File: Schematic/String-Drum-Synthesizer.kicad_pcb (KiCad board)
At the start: 2 copper layers, 62 parts, among them U1 LM1117MP-3.3, U2 SII1136CTU, U4 LM3900DR, U5 LM1117MP-3.3, U6 STM32F722RCTx

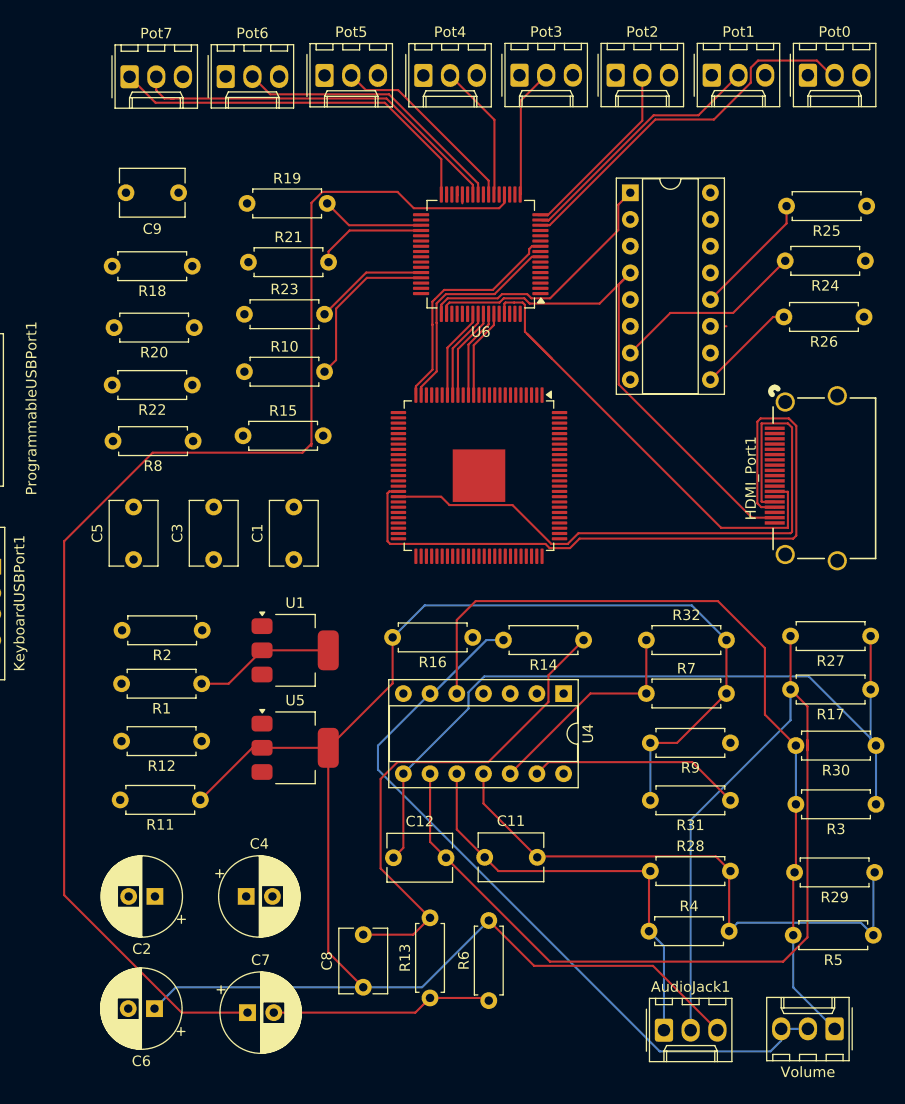
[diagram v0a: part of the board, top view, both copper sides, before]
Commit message: Deleted old traces
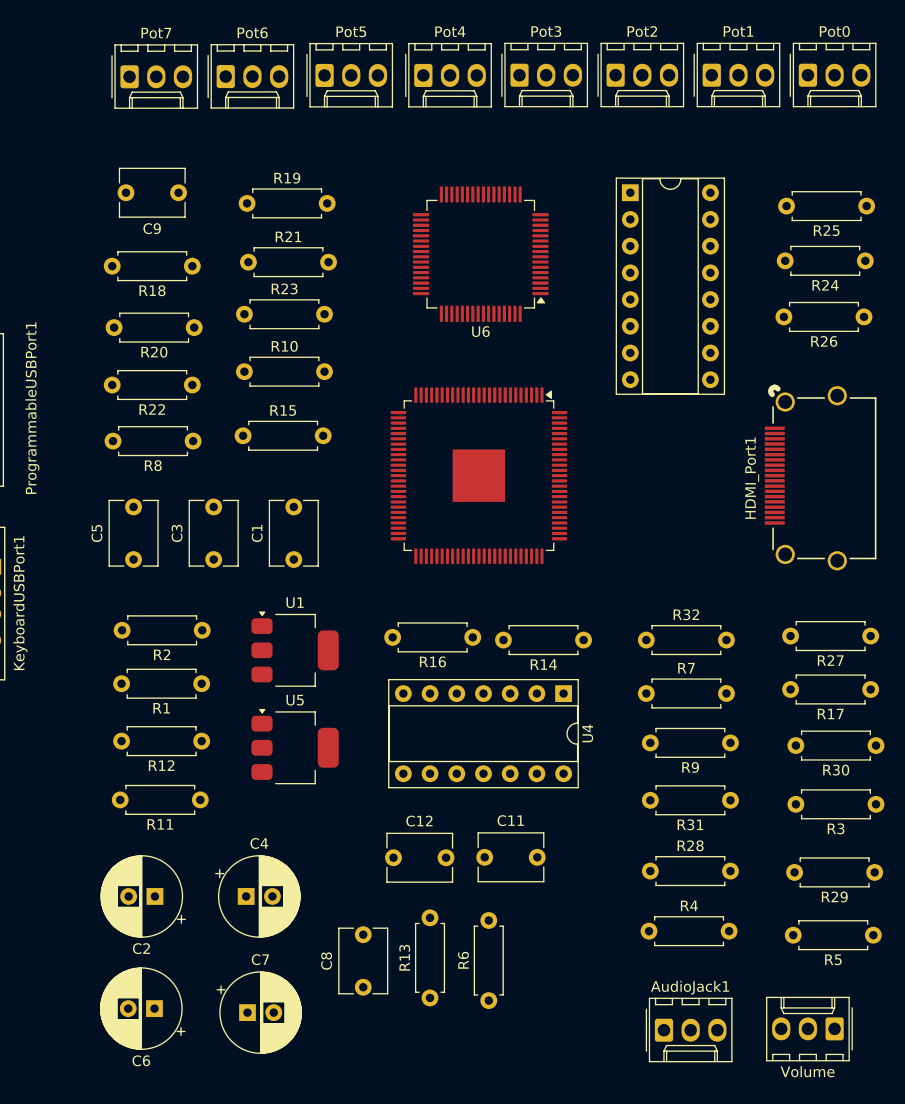
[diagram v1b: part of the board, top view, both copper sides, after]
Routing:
- net +2V5: track 168.1 -> 0.00 mm
- net /DAC Out: track 126.7 -> 0.00 mm
- net /Audio Out R: track 114.7 -> 0.00 mm
- net /AmplifiedSignal: track 78.1 -> 0.00 mm
- net Net-(U4-3IN-): track 77.3 -> 0.00 mm
- net Net-(Pot8-Pin_2): track 72.2 -> 0.00 mm
- net /DSDA: track 69.5 -> 0.00 mm
- net /DSCL: track 61.5 -> 0.00 mm
- net Net-(U4-IN4-): track 55.6 -> 0.00 mm
- net /HDMI_PWR: track 51.1 -> 0.00 mm
- net +3V3: track 49.6 -> 0.00 mm
- net Net-(C8-Pad2): track 48.4 -> 0.00 mm
- net /PB8: track 46.3 -> 0.00 mm
- net /Audio Out L: track 41.3 -> 0.00 mm
- net /EmotiveKnobValue7: track 36.3 -> 0.00 mm
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
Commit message: SCHEMATIC COMPLETE
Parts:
- removed 74LS257: 74LS257, Package_DIP:DIP-16_W7.62mm_Socket
- removed R26: 1M, Resistor_THT:R_Axial_DIN0207_L6.3mm_D2.5mm_P7.62mm_Horizontal
- added R33: 5.6k, Resistor_THT:R_Axial_DIN0207_L6.3mm_D2.5mm_P7.62mm_Horizontal, F.Cu at (145.9, 76.2)
- R24: value 1M -> 4k7
- R25: value 1M -> 10k
- moved R17 22.7 mm to (168.3, 129.3)
- moved R27 22.7 mm to (168.3, 124.2)
- moved Volume 21.3 mm to (143.6, 138.4)
- moved R24 15.0 mm to (156.5, 56.0), turned to 0 degrees
- moved R5 11.7 mm to (167.6, 118.2)
- moved R29 11.7 mm to (167.8, 112.3)
- moved R25 11.6 mm to (156.5, 60.1), turned to 0 degrees
- moved R30 10.5 mm to (167.5, 101.5)
- moved R3 10.5 mm to (167.5, 107.1)
- moved KeyboardUSBPort1 9.31 mm to (82.3, 107.7)
- moved R1 0.85 mm to (104.8, 105.2)
- moved HDMI_Port1 0.83 mm to (164.7, 86.0)
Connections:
- net /PC13 renamed /NRESET
- HDMI_Port1 pad 1: /PB6 -> /TX2+
- HDMI_Port1 pad 10: /PB10 -> /TXC+
- HDMI_Port1 pad 11: unconnected-(HDMI_Port1-Pad11) -> GND
- HDMI_Port1 pad 12: /PB11 -> /TXC-
- HDMI_Port1 pad 18: /HDMI_PWR -> +5V
- HDMI_Port1 pad 19: unconnected-(HDMI_Port1-Pad19) -> Net-(HDMI_Port1-Pad19)
- HDMI_Port1 pad 2: unconnected-(HDMI_Port1-Pad2) -> GND
- HDMI_Port1 pad 3: /PB7 -> /TX2-
- HDMI_Port1 pad 4: /PB4 -> /TX1+
- HDMI_Port1 pad 5: unconnected-(HDMI_Port1-Pad5) -> GND
- HDMI_Port1 pad 6: /PB5 -> /TX1-
- HDMI_Port1 pad 7: /PB2 -> /TX0+
- HDMI_Port1 pad 8: unconnected-(HDMI_Port1-Pad8) -> GND
- HDMI_Port1 pad 9: /PB3 -> /TX0-
- R24 pad 1: GND -> /HPD_IN
- R24 pad 2: Net-(U3-Zb) -> Net-(HDMI_Port1-Pad19)
- R25 pad 2: Net-(U3-Zc) -> /HPD_IN
- U2 pad 10: unconnected-(U2-D8-Pad10) -> GND
- U2 pad 11: /PB11 -> /PB9
- U2 pad 13: /PB10 -> /PB8
- U2 pad 2: unconnected-(U2-D15-Pad2) -> GND
- U2 pad 22: unconnected-(U2-IDCK-Pad22) -> /IDCK
- U2 pad 23: /PC1 -> /VSYNC
- U2 pad 24: /PC0 -> /HSYNC
- U2 pad 25: /PC2 -> /DE
- U2 pad 3: unconnected-(U2-D14-Pad3) -> GND
- U2 pad 4: unconnected-(U2-D13-Pad4) -> GND
- U2 pad 52: unconnected-(U2-EXT_SWING-Pad52) -> Net-(U2-EXT_SWING)
- U2 pad 54: unconnected-(U2-TXC--Pad54) -> /TXC-
- U2 pad 55: unconnected-(U2-TXC+-Pad55) -> /TXC+
- U2 pad 57: unconnected-(U2-TX0--Pad57) -> /TX0-
- U2 pad 58: unconnected-(U2-TX0+-Pad58) -> /TX0+
- U2 pad 59: unconnected-(U2-TX1--Pad59) -> /TX1-
- U2 pad 6: unconnected-(U2-D12-Pad6) -> GND
- U2 pad 60: unconnected-(U2-TX1+-Pad60) -> /TX1+
- U2 pad 62: unconnected-(U2-TX2--Pad62) -> /TX2-
- U2 pad 63: unconnected-(U2-TX2+-Pad63) -> /TX2+
- U2 pad 7: unconnected-(U2-D11-Pad7) -> GND
- U2 pad 76: unconnected-(U2-HPD-Pad76) -> /HPD_OUT
- U2 pad 78: unconnected-(U2-D35-Pad78) -> GND
- U2 pad 79: unconnected-(U2-D34-Pad79) -> GND
- U2 pad 8: unconnected-(U2-D10-Pad8) -> GND
- U2 pad 80: unconnected-(U2-D33-Pad80) -> GND
- U2 pad 81: unconnected-(U2-D32-Pad81) -> GND
- U2 pad 82: unconnected-(U2-D31-Pad82) -> GND
- U2 pad 83: unconnected-(U2-D30-Pad83) -> GND
- U2 pad 84: unconnected-(U2-D29-Pad84) -> GND
- U2 pad 85: unconnected-(U2-D28-Pad85) -> GND
- U2 pad 86: unconnected-(U2-D27-Pad86) -> GND
- U2 pad 87: unconnected-(U2-D26-Pad87) -> GND
- U2 pad 89: unconnected-(U2-D25-Pad89) -> GND
- U2 pad 9: unconnected-(U2-D9-Pad9) -> GND
- U2 pad 90: unconnected-(U2-D24-Pad90) -> GND
- U2 pad 92: unconnected-(U2-D23-Pad92) -> GND
- U2 pad 93: unconnected-(U2-D22-Pad93) -> GND
- U2 pad 94: unconnected-(U2-D21-Pad94) -> GND
- U2 pad 95: unconnected-(U2-D20-Pad95) -> GND
- U2 pad 96: unconnected-(U2-D19-Pad96) -> GND
- U2 pad 97: unconnected-(U2-D18-Pad97) -> GND
- U2 pad 98: unconnected-(U2-D17-Pad98) -> GND
- U2 pad 99: unconnected-(U2-D16-Pad99) -> GND
- U6 pad 10: /PC2 -> /VSYNC
- U6 pad 28: /PB10 -> /IDCK
- U6 pad 29: /PB11 -> /HPD_IN
- U6 pad 33: unconnected-(U6-PB12-Pad33) -> /HPD_OUT
- U6 pad 49: /HDMI_PWR_SELECT -> unconnected-(U6-PA14-Pad49)
- U6 pad 50: /HDMI_PWR -> unconnected-(U6-PA15-Pad50)
- U6 pad 8: /PC0 -> /DE
- U6 pad 9: /PC1 -> /HSYNC
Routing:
- added copper zone on F.Cu, net GND

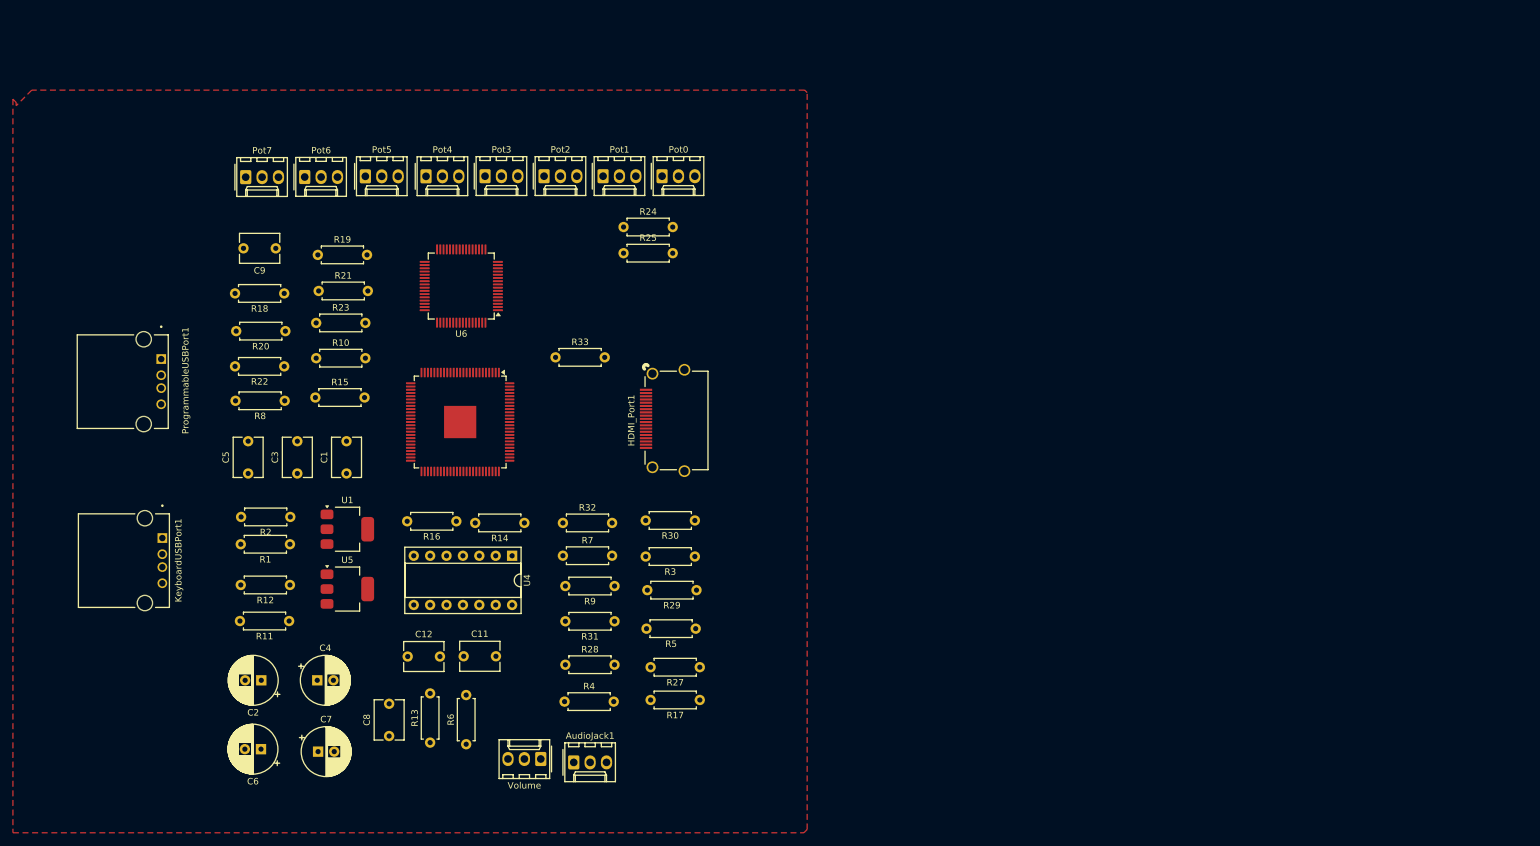
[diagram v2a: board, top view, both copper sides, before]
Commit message: Half the copper traces work
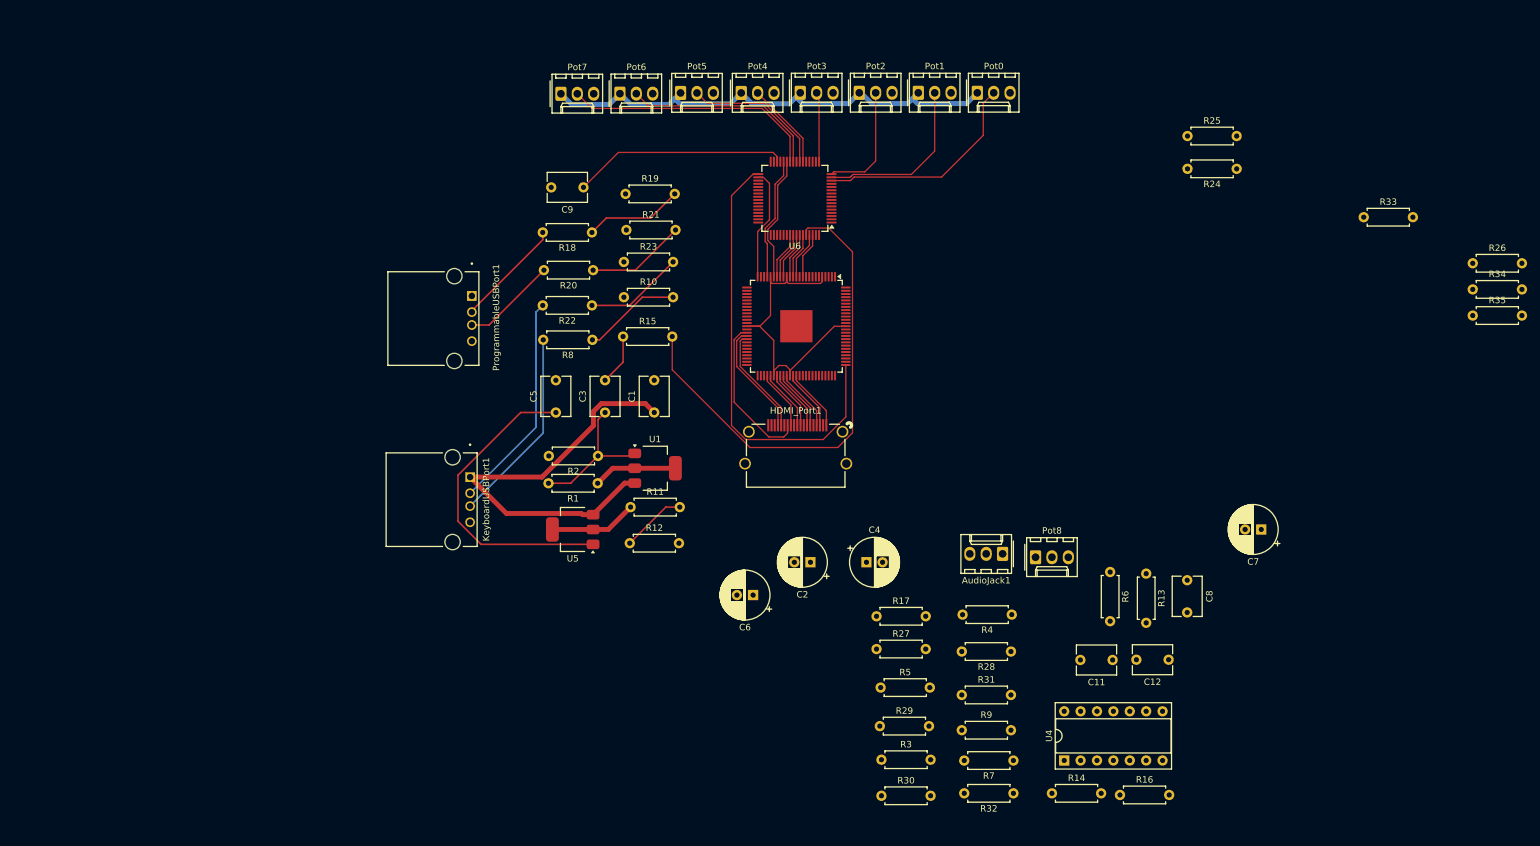
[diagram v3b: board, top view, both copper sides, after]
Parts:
- added R26: 10k, Resistor_THT:R_Axial_DIN0207_L6.3mm_D2.5mm_P7.62mm_Horizontal, F.Cu at (288.0, 61.6)
- added R34: 5k6, Resistor_THT:R_Axial_DIN0207_L6.3mm_D2.5mm_P7.62mm_Horizontal, F.Cu at (288.0, 65.7)
- added R35: 10k, Resistor_THT:R_Axial_DIN0207_L6.3mm_D2.5mm_P7.62mm_Horizontal, F.Cu at (288.0, 69.7)
- moved C7 150.1 mm to (255.3, 102.9), turned to 180 degrees
- moved R33 127.1 mm to (271.1, 54.5)
- moved C8 126.0 mm to (243.8, 110.7), turned to -90 degrees
- moved C12 117.9 mm to (240.9, 123.0), turned to 180 degrees
- moved R13 114.0 mm to (237.4, 109.7), turned to -90 degrees
- moved R16 111.2 mm to (233.4, 144.0), turned to 0 degrees
- moved R6 103.3 mm to (231.9, 109.5), turned to -90 degrees
- moved C11 100.6 mm to (232.2, 123.1), turned to 180 degrees
- moved R24 95.4 mm to (251.5, 47.0), turned to 180 degrees
- moved R14 91.9 mm to (222.8, 143.7), turned to 0 degrees
- moved U4 91.2 mm to (224.7, 138.7), turned to 90 degrees
- moved R25 89.2 mm to (243.8, 41.9)
- moved C4 87.0 mm to (194.1, 108.0)
- moved C2 87.0 mm to (185.4, 108.0)
- moved Pot8 82.8 mm to (220.3, 107.2), turned to 0 degrees
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- renumbered Volume to Pot8
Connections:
- U2 pad 16: +3.3V -> Net-(U2-AVCC)
- U2 pad 21: +3.3V -> Net-(U2-AVCC)
- U2 pad 23: /VSYNC -> unconnected-(U2-VSYNC-Pad23)
- U2 pad 24: /HSYNC -> unconnected-(U2-HSYNC-Pad24)
- U2 pad 38: +3.3V -> Net-(U2-AVCC)
- U2 pad 47: /NRESET -> Net-(U2-~{RESET})
- U2 pad 5: +3.3V -> Net-(U2-AVCC)
- U2 pad 56: +3.3V -> Net-(U2-AVCC)
- U2 pad 61: +3.3V -> Net-(U2-AVCC)
- U2 pad 88: +3.3V -> Net-(U2-AVCC)
- U6 pad 10: /VSYNC -> unconnected-(U6-PC2-Pad10)
- U6 pad 2: /NRESET -> unconnected-(U6-PC13-Pad2)
- U6 pad 34: unconnected-(U6-PB13-Pad34) -> /DE
- U6 pad 8: /DE -> unconnected-(U6-PC0-Pad8)
- U6 pad 9: /HSYNC -> unconnected-(U6-PC1-Pad9)
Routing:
- net +3V3: track 0.00 -> 88.7 mm
- net Net-(U6-BOOT0): track 0.00 -> 76.7 mm
- net /HPD_OUT: track 0.00 -> 69.2 mm
- net +5V: track 0.00 -> 65.1 mm
- net Net-(U5-GND): track 0.00 -> 58.8 mm
- net Net-(U2-AVCC): track 0.00 -> 46.9 mm
- net /EmotiveKnobValue7: track 0.00 -> 39.6 mm
- net Net-(KeyboardUSBPort1-D-): track 0.00 -> 33.8 mm
- net /EmotiveKnobValue0: track 0.00 -> 33.7 mm
- net Net-(U6-VCAP_1): track 0.00 -> 33.3 mm
- net /EmotiveKnobValue6: track 0.00 -> 31.0 mm
- net Net-(KeyboardUSBPort1-D+): track 0.00 -> 30.5 mm
- net /EmotiveKnobValue1: track 0.00 -> 26.7 mm
- net /CEC_A: track 0.00 -> 24.1 mm
- net Net-(U1-GND): track 0.00 -> 22.5 mm
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- removed copper zone on F.Cu, net GND

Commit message: Hopefully this layout is good
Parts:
- moved C12 123.4 mm to (117.5, 125.5), turned to 0 degrees
- moved Op-Amp 112.8 mm to (129.3, 78.6), turned to 0 degrees
- moved Pot8 103.4 mm to (118.1, 91.6)
- moved C11 98.1 mm to (134.2, 125.3)
- moved AudioJack1 92.1 mm to (123.2, 101.7)
- moved R35 88.8 mm to (199.4, 74.1)
- moved R34 81.2 mm to (207.0, 60.8), turned to 180 degrees
- moved R26 80.9 mm to (207.3, 67.0), turned to 180 degrees
- moved R30 80.2 mm to (129.5, 99.9)
- moved R17 78.8 mm to (117.0, 112.9)
- moved R27 78.6 mm to (117.1, 118.0)
- moved R3 74.2 mm to (129.5, 106.3)
- moved R33 72.8 mm to (199.1, 43.7)
- moved R5 68.6 mm to (129.2, 113.3)
- moved R7 68.2 mm to (150.1, 124.7)
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- renumbered U4 to Op-Amp
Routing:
- net +3V3: track 88.7 -> 13.0 mm
- net /HPD_OUT: track 69.2 -> 135.2 mm
- net Net-(U6-BOOT0): track 76.7 -> 142.0 mm
- net Net-(U5-GND): track 58.8 -> 10.1 mm
- net /EmotiveKnobValue7: track 39.6 -> 0.00 mm
- net /EmotiveKnobValue0: track 33.7 -> 0.00 mm
- net /TXC+: track 9.40 -> 42.8 mm
- net /TXC-: track 9.19 -> 42.2 mm
- net /TX2-: track 9.40 -> 42.4 mm
- net /TX2+: track 9.60 -> 42.6 mm
- net /TX1-: track 9.40 -> 42.4 mm
- net /TX1+: track 9.60 -> 42.6 mm
- net /TX0-: track 9.19 -> 42.2 mm
- net /TX0+: track 9.40 -> 42.4 mm
- net /DSDA: track 17.6 -> 50.6 mm
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
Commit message: Is it done?
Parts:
- added H1: MountingHole, MountingHole:MountingHole_3.2mm_M3, F.Cu at (121.2, 29.0)
- added H2: MountingHole, MountingHole:MountingHole_3.2mm_M3, F.Cu at (204.5, 28.1)
- added H3: MountingHole, MountingHole:MountingHole_3.2mm_M3, F.Cu at (119.8, 136.5)
- added H4: MountingHole, MountingHole:MountingHole_3.2mm_M3, F.Cu at (208.7, 133.5)
- moved R13 33.4 mm to (207.1, 80.4), turned to -90 degrees
- moved Pot3 8.28 mm to (169.5, 36.3)
- moved Pot5 8.28 mm to (151.0, 36.3)
- moved Pot6 8.28 mm to (141.6, 36.4)
- moved Pot0 8.28 mm to (197.0, 36.3)
- moved Pot1 8.28 mm to (187.8, 36.3)
- moved Pot2 8.28 mm to (178.7, 36.3)
- moved Pot4 8.28 mm to (160.4, 36.3)
- moved Pot7 8.28 mm to (132.5, 36.4)
- moved R16 8.26 mm to (207.1, 102.6)
- moved C8 7.03 mm to (207.4, 97.8)
- moved C7 4.56 mm to (198.2, 84.7), turned to 90 degrees
- moved ProgrammableUSBPort1 4.15 mm to (122.6, 47.3)
- moved HDMI_Port1 3.23 mm to (183.1, 127.6)
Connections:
- C11 pad 2: Net-(U4-IN4-) -> Net-(Op-Amp1-IN4-)
- C12 pad 1: Net-(U4-3IN-) -> Net-(Op-Amp1-3IN-)
- Pot8 pad 2: Net-(Pot8-Pin_2) -> Net-(Op-Amp1-1IN-)
- Pot8 pad 3: Net-(Pot8-Pin_2) -> Net-(Op-Amp1-1IN-)
- R14 pad 2: Net-(Pot8-Pin_2) -> Net-(Op-Amp1-1IN-)
- R16 pad 1: Net-(U4-1IN+) -> Net-(Op-Amp1-1IN+)
- R17 pad 1: Net-(U4-3IN-) -> Net-(Op-Amp1-3IN-)
- R27 pad 1: Net-(U4-3IN-) -> Net-(Op-Amp1-3IN-)
- R28 pad 2: Net-(U4-IN4-) -> Net-(Op-Amp1-IN4-)
- R29 pad 1: Net-(U4-IN4-) -> Net-(Op-Amp1-IN4-)
- R3 pad 1: Net-(U4-3IN-) -> Net-(Op-Amp1-3IN-)
- R30 pad 1: Net-(U4-3IN-) -> Net-(Op-Amp1-3IN-)
- R31 pad 1: Net-(U4-3IN+) -> Net-(Op-Amp1-3IN+)
- R32 pad 1: Net-(U4-4IN+) -> Net-(Op-Amp1-4IN+)
- R4 pad 2: Net-(U4-IN4-) -> Net-(Op-Amp1-IN4-)
- R5 pad 1: Net-(U4-IN4-) -> Net-(Op-Amp1-IN4-)
- R7 pad 1: Net-(U4-4IN+) -> Net-(Op-Amp1-4IN+)
- R9 pad 1: Net-(U4-3IN+) -> Net-(Op-Amp1-3IN+)
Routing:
- net +2V5: track 13.6 -> 209.2 mm
- net /Audio Out L: track 0.00 -> 108.4 mm
- net Net-(C7-Pad2): track 0.00 -> 67.5 mm
- net Net-(Op-Amp1-1IN-): track 0.00 -> 64.7 mm
- net Net-(C8-Pad2): track 0.00 -> 60.5 mm
- net /Audio Out R: track 0.00 -> 54.9 mm
- net /AmplifiedSignal: track 0.00 -> 53.5 mm
- net /EmotiveKnobValue7: track 0.00 -> 51.7 mm
- net +5V: track 34.3 -> 80.8 mm
- net /EmotiveKnobValue6: track 0.00 -> 45.6 mm
- net Net-(Op-Amp1-3IN-): track 0.00 -> 45.2 mm
- net /EmotiveKnobValue5: track 0.00 -> 37.1 mm
- net Net-(Op-Amp1-IN4-): track 0.00 -> 32.1 mm
- net Net-(U5-GND): track 10.1 -> 41.9 mm
- net /EmotiveKnobValue4: track 0.00 -> 27.5 mm
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- added copper zone on B.Cu, net +3V3
- added copper zone on F.Cu, net GND
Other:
- board text added: "Team 21 Oct 2024 Version 1"

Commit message: Yes it is done
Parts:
- removed HDMI_Port1: 10029449-111RLF, 10029449_111RLF:CONN_10029449111_AMP
- added J1: HDMI_A_1.4, Connector_Video:HDMI_A_Molex_208658-1001_Horizontal, F.Cu at (183.3, 125.8)
- moved H3 6.56 mm to (115.1, 132.0)
- moved H1 5.64 mm to (115.7, 30.4)
- moved H2 4.19 mm to (207.9, 30.5)
- moved R2 1.43 mm to (152.5, 90.0)
- moved H4 1.08 mm to (209.4, 132.7)
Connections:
- R26 pad 1: +3.3V -> +3V3
- R35 pad 2: +3.3V -> +3V3
- U2 pad 1: +3.3V -> +3V3
- U2 pad 12: +3.3V -> +3V3
- U2 pad 37: +3.3V -> +3V3
- U2 pad 91: +3.3V -> +3V3
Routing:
- net GND: track 7.93 -> 113.3 mm
- net +5V: track 80.8 -> 85.0 mm
- net Net-(U5-GND): track 41.9 -> 45.8 mm
- net Net-(C7-Pad2): track 67.5 -> 71.0 mm
- net /Audio Out L: track 108.4 -> 111.6 mm
- net /CEC_A: track 59.8 -> 62.9 mm
- net /EmotiveKnobValue5: track 37.1 -> 34.8 mm
- net /EmotiveKnobValue6: track 45.6 -> 43.3 mm
- net Net-(U6-BOOT0): track 148.5 -> 150.3 mm
- net +2V5: track 209.2 -> 211.0 mm
- net /HPD_OUT: track 141.6 -> 143.2 mm
- net /EmotiveKnobValue4: track 27.5 -> 25.9 mm
- net /USB_OTG_FS_DP: track 15.4 -> 16.4 mm
- net /TXC+: track 45.6 -> 46.6 mm
- net Net-(U1-GND): track 22.5 -> 23.3 mm
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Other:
- board outline added: 101 x 108.1 mm
